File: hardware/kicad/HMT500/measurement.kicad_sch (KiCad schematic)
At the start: 15 parts, among them J3 Feedthrough 6P, U5 PCAP04-AQFM-24, U6 ADS1220IPWR

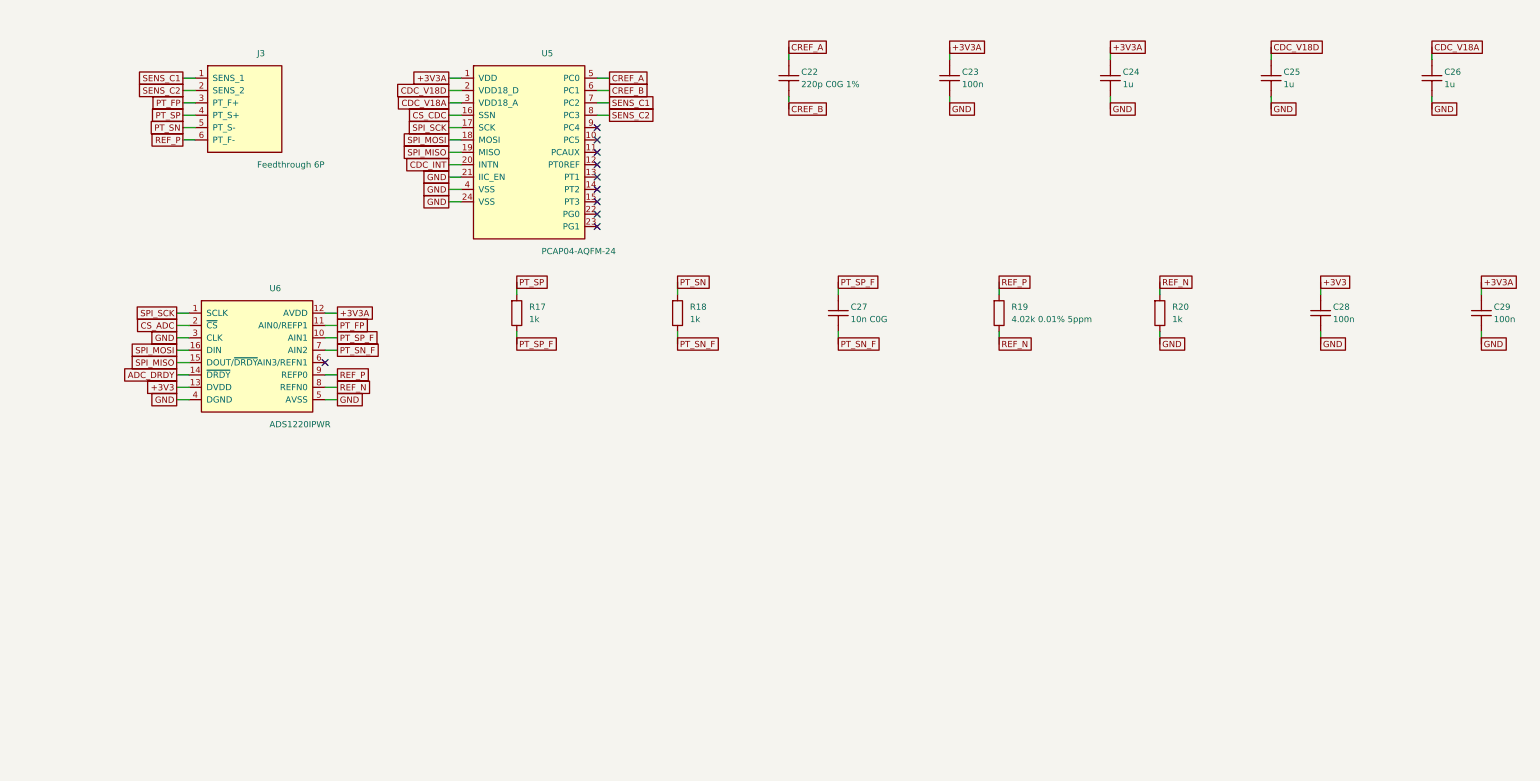
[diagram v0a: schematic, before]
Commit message: KiCad schematic v0.2: hand-laid-out, wired, readable sheets with power symbols and functional blocks
Replaces the label-only v0.1. Drawing rules are validated at generation and
the drawn netlist is checked against design intent (71 nets, 0 errors).

Co-Authored-By: Claude Opus 5.5 <noreply@anthropic.com>
Claude-Session: https://claude.ai/code/session_01JA2o8uJsqp9Vzsg4b665ev
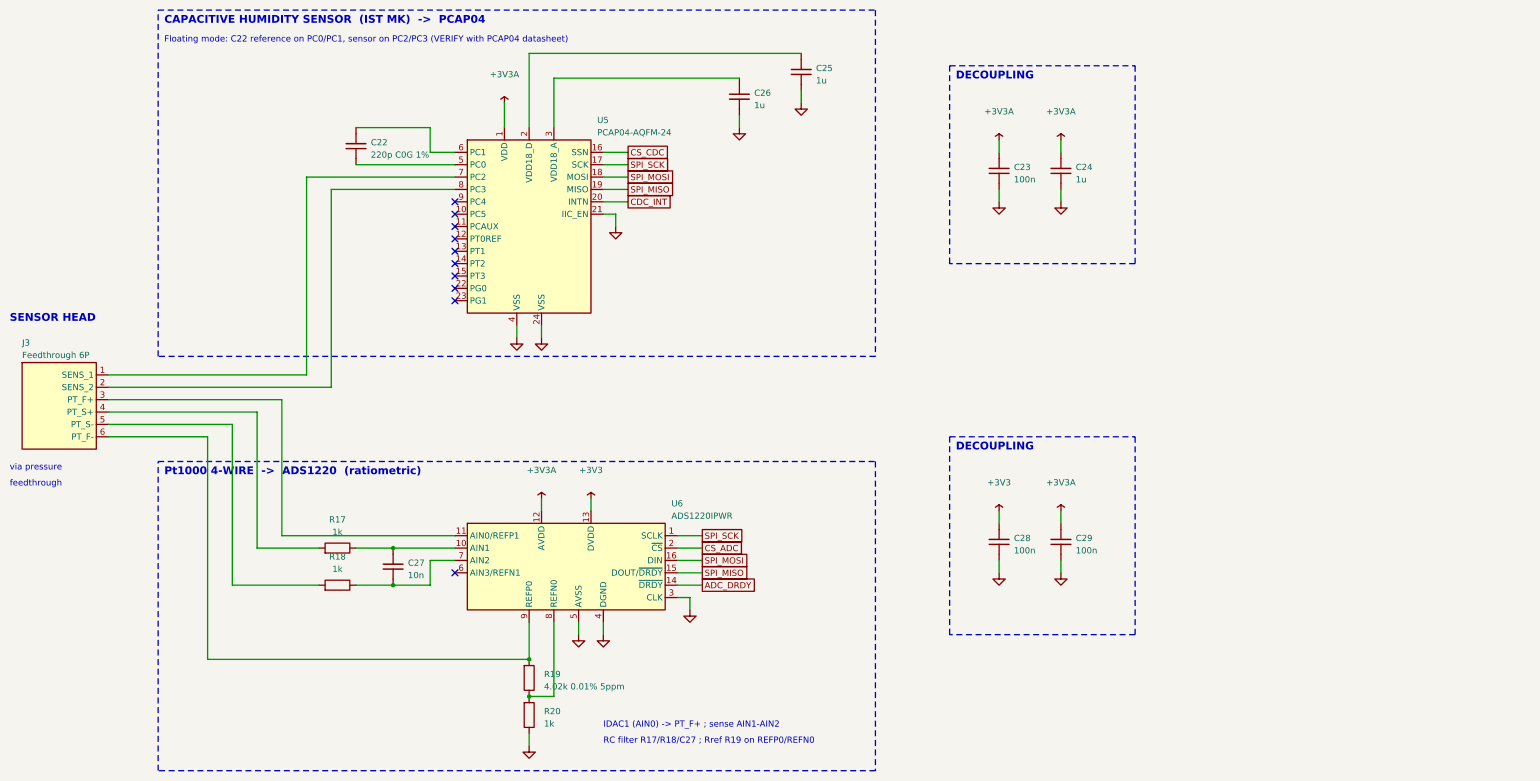
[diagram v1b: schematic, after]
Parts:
- C27: value 10n C0G -> 10n
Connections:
- net CDC_V18A: no longer names the net of C26.1, U5.3 (VDD18_A)
- net CDC_V18D: no longer names the net of C25.1, U5.2 (VDD18_D)
- net CREF_A: no longer names the net of C22.1
- net CREF_A: now also U5.6 (PC1); no longer U5.5 (PC0)
- net CREF_B: no longer names the net of C22.2
- net CREF_B: now also U5.5 (PC0); no longer U5.6 (PC1)
- net PT_FP: no longer names the net of J3.3 (PT_F+), U6.11 (AIN0/REFP1)
- net PT_SN: no longer names the net of J3.5 (PT_S-), R18.1
- net PT_SN_F: no longer names the net of C27.2, R18.2, U6.7 (AIN2)
- net PT_SP: no longer names the net of J3.4 (PT_S+), R17.1
- net PT_SP_F: no longer names the net of C27.1, R17.2, U6.10 (AIN1)
- net REF_N: no longer names the net of R19.2, R20.1, U6.8 (REFN0)
- net REF_P: no longer names the net of J3.6 (PT_F-), R19.1, U6.9 (REFP0)
- net SENS_C1: no longer names the net of J3.1 (SENS_1), U5.7 (PC2)
- net SENS_C2: no longer names the net of J3.2 (SENS_2), U5.8 (PC3)
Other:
- note added: "CAPACITIVE HUMIDITY SENSOR (IST MK) -> PCAP04"
- note added: "DECOUPLING"
- note added: "Floating mode: C22 reference on PC0/PC1, sensor on PC2/PC3 (VERIFY with PCAP04 datasheet)"
- note added: "IDAC1 (AIN0) -> PT_F+ ; sense AIN1-AIN2"
- note added: "Pt1000 4-WIRE -> ADS1220 (ratiometric)"
- note added: "RC filter R17/R18/C27 ; Rref R19 on REFP0/REFN0"
- note added: "SENSOR HEAD"
- note added: "feedthrough"
- note added: "via pressure"
- title: HMT500 - Capacitance (PCAP04) and Pt1000 (ADS1220) -> HMT500  Measurement
- moved on the sheet: C22, C23, C24, C25, C26, C27, C28, C29, J3, R17, R18, R19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

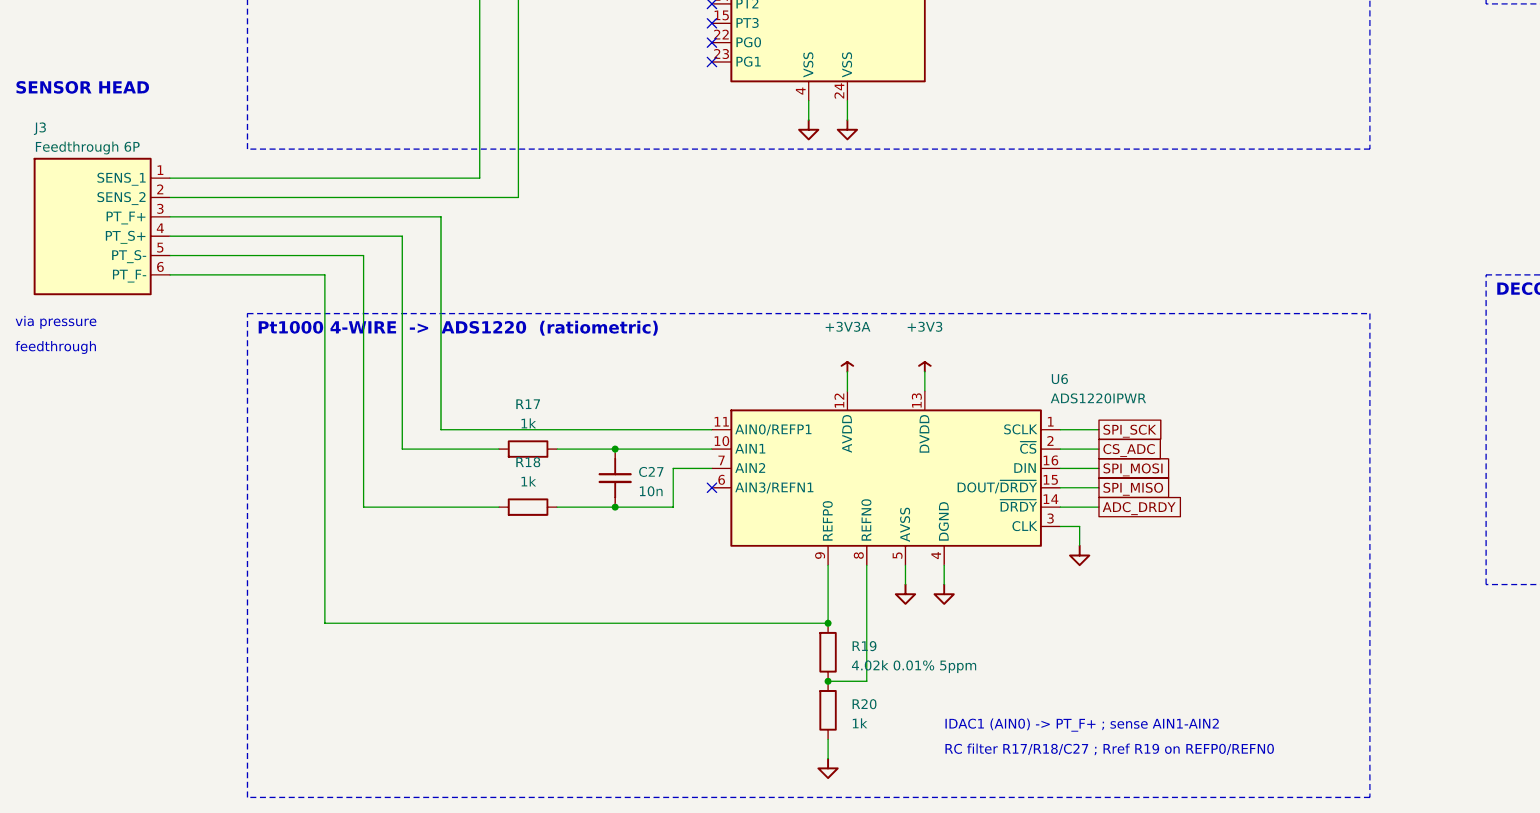
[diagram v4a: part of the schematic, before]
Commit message: Sensor harness W-1: JST SH 1.0 mm 4P between feedthrough and PCB J3
- Schematic v0.4: J3 = BM04B-SRSS-TB (top entry). Pins 1-2 MK33, 3-4 Pt1000
  2-wire with force/sense split at the J3 pads (68 nets, netlist check 0 errors)
- Parts list: J3 header, SHR-04V-S housing, SSH-003T-P0.2-H contacts, PTFE AWG30 wire
- Mech: J3 and harness in params/CAD/drawings (item 17, notes 5 and 9), PCAP04
  moved directly behind J3, PCB outline and KiCad board zone updated
- Test for harness clearance, J3 height and pin mapping
- Decision log #16; JST SH -25..+85 C rating added to open items

Co-Authored-By: Claude Opus 5.5 <noreply@anthropic.com>
Claude-Session: https://claude.ai/code/session_01JA2o8uJsqp9Vzsg4b665ev
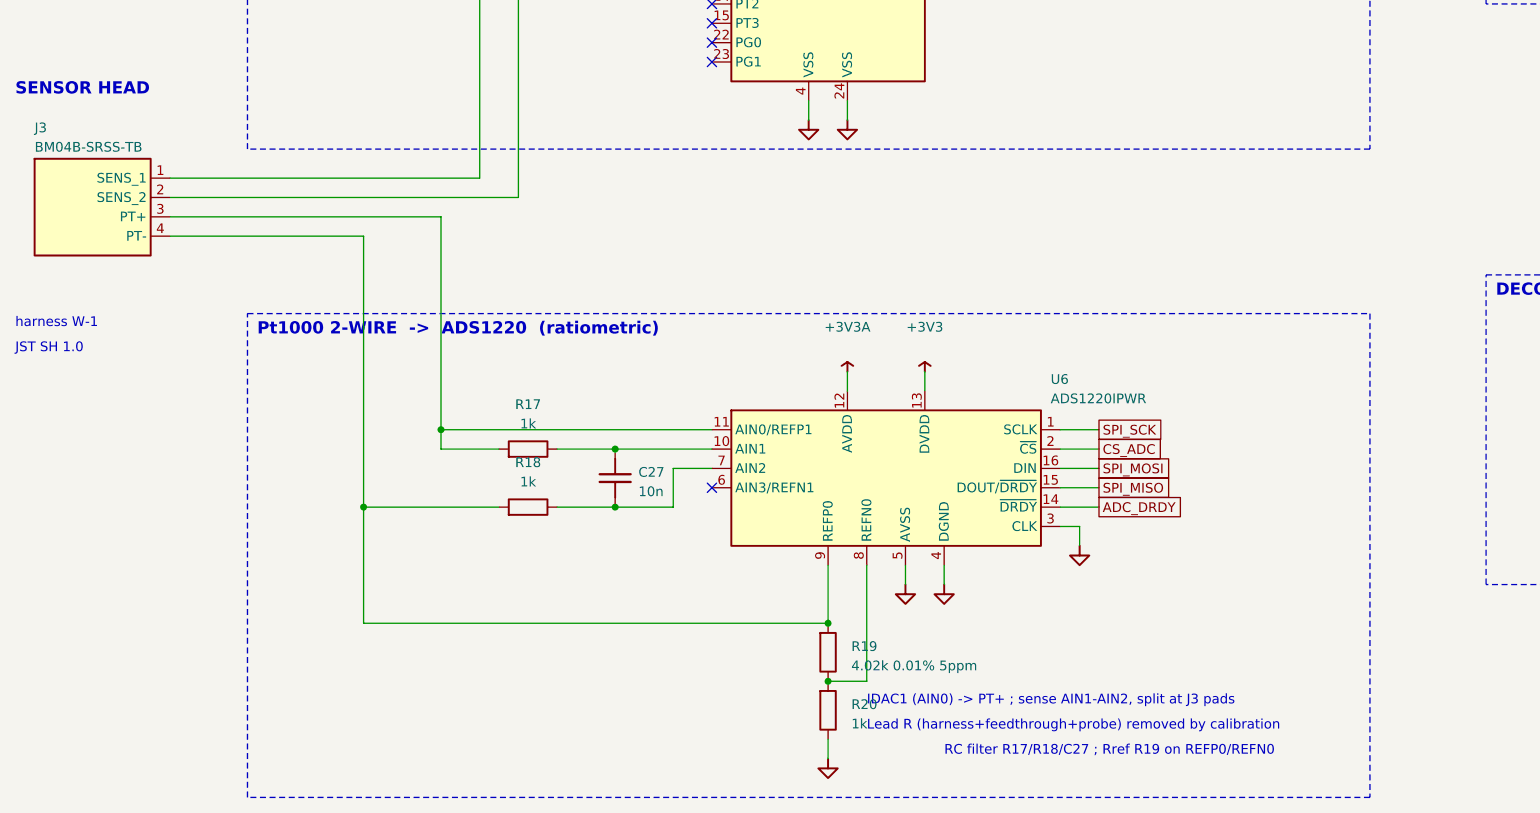
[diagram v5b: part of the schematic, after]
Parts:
- J3: value Feedthrough 6P -> BM04B-SRSS-TB; footprint TBD:Feedthrough_6P -> Connector_JST:JST_SH_BM04B-SRSS-TB_1x04-1MP_P1.00mm_Vertical; symbol HMT500:CONN_PROBE -> HMT500:CONN_SH4
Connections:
- net at J3.3 (PT+), U6.11 (AIN0/REFP1): now also R17.1
- net at R19.1, U6.9 (REFP0): now also J3.4 (PT-), R18.1; no longer J3.6 (PT_F-)
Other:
- note added: "IDAC1 (AIN0) -> PT+ ; sense AIN1-AIN2, split at J3 pads"
- note added: "JST SH 1.0"
- note added: "Lead R (harness+feedthrough+probe) removed by calibration"
- note added: "Pt1000 2-WIRE -> ADS1220 (ratiometric)"
- note added: "harness W-1"
- note removed: "IDAC1 (AIN0) -> PT_F+ ; sense AIN1-AIN2"
- note removed: "Pt1000 4-WIRE -> ADS1220 (ratiometric)"
- note removed: "feedthrough"
- note removed: "via pressure"
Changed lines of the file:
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@@
 (kicad_sch (version 20230121) (generator eeschema) (paper "A3")
-(title_block (title "HMT500  Measurement") (date "2026-09-26") (rev "0.3") (company "DOTECH Co., Ltd.") (comment 1 "Oil moisture transmitter HMT500 - RS-485 + 2x V/I analog output") (comment 2 "Design notes: docs/hw/circuit-design.md") (comment 3 "VERIFY=YES parts: pin numbers LMR36006/PCAP04/DAC8760/TPS26611; TPS2660 R22"))
-(symbol (lib_id "HMT500:CONN_PROBE") (at 25.4 106.68 0) (unit 1) (in_bom yes) (on_board yes) (dnp no) (property "Reference" "J3" (at 17.78 94.996 0) (effects (font (size 1.27 1.27)) (justify left))) (property "Value" "Feedthrough 6P" (at 17.78 97.536 0) (effects (font (size 1.27 1.27)) (justify left))) (property "Footprint" "TBD:Feedthrough_6P" (at 25.4 106.68 0) (effects (font (size 1.27 1.27)) hide)) (property "Datasheet" "~" (at 25.4 106.68 0) (effects (font (size 1.27 1.27)) hide)) (pin "1") (pin "2") (pin "3") (pin "4") (pin "5") (pin "6") (instances (project "HMT500" (path "/1ebb025b-11bd-5f7c-aaab-41e2a750e8b3/3db4a209-237d-57e2-bca4-a1eda7d94116" (reference "J3") (unit 1)))))
+(title_block (title "HMT500  Measurement") (date "2026-09-29") (rev "0.4") (company "DOTECH Co., Ltd.") (comment 1 "Oil moisture transmitter HMT500 - RS-485 + 2x V/I analog output") (comment 2 "Design notes: docs/hw/circuit-design.md") (comment 3 "VERIFY=YES parts: pin numbers LMR36006/PCAP04/DAC8760/TPS26611; TPS2660 R22"))
+(symbol (lib_id "HMT500:CONN_SH4") (at 25.4 104.14 0) (unit 1) (in_bom yes) (on_board yes) (dnp no) (property "Reference" "J3" (at 17.78 94.996 0) (effects (font (size 1.27 1.27)) (justify left))) (property "Value" "BM04B-SRSS-TB" (at 17.78 97.536 0) (effects (font (size 1.27 1.27)) (justify left))) (property "Footprint" "Connector_JST:JST_SH_BM04B-SRSS-TB_1x04-1MP_P1.00mm_Vertical" (at 25.4 104.14 0) (effects (font (size 1.27 1.27)) hide)) (property "Datasheet" "~" (at 25.4 104.14 0) (effects (font (size 1.27 1.27)) hide)) (pin "1") (pin "2") (pin "3") (pin "4") (instances (project "HMT500" (path "/1ebb025b-11bd-5f7c-aaab-41e2a750e8b3/3db4a209-237d-57e2-bca4-a1eda7d94116" (reference "J3") (unit 1)))))
 (symbol (lib_id "HMT500:PCAP04") (at 121.92 71.12 0) (unit 1) (in_bom yes) (on_board yes) (dnp no) (property "Reference" "U5" (at 135.89 49.276 0) (effects (font (size 1.27 1.27)) (justify left))) (property "Value" "PCAP04-AQFM-24" (at 135.89 51.816 0) (effects (font (size 1.27 1.27)) (justify left))) (property "Footprint" "TBD:QFN-24_PCAP04" (at 121.92 71.12 0) (effects (font (size 1.27 1.27)) hide)) (property "Datasheet" "~" (at 121.92 71.12 0) (effects (font (size 1.27 1.27)) hide)) (property "VERIFY" "YES - pin numbers are placeholders" (at 121.92 71.12 0) (effects (font (size 1.27 1.27)) hide)) (pin "6") (pin "5") (pin "7") (pin "8") (pin "9") (pin "10") (pin "11") (pin "12") (pin "13") (pin "14") (pin "15") (pin "22") (pin "23") (pin "16") (pin "17") (pin "18") (pin "19") (pin "20") (pin "21") (pin "1") (pin "2") (pin "3") (pin "4") (pin "24") (instances (project "HMT500" (path "/1ebb025b-11bd-5f7c-aaab-41e2a750e8b3/3db4a209-237d-57e2-bca4-a1eda7d94116" (reference "U5") (unit 1)))))
 (symbol (lib_id "HMT500:C") (at 86.36 54.61 0) (unit 1) (in_bom yes) (on_board yes) (dnp no) (property "Reference" "C22" (at 89.408 53.848 0) (effects (font (size 1.27 1.27)) (justify left))) (property "Value" "220p C0G 1%" (at 89.408 56.388 0) (effects (font (size 1.27 1.27)) (justify left))) (property "Footprint" "Capacitor_SMD:C_0603_1608Metric" (at 86.36 54.61 0) (effects (font (size 1.27 1.27)) hide)) (property "Datasheet" "~" (at 86.36 54.61 0) (effects (font (size 1.27 1.27)) hide)) (pin "1") (pin "2") (instances (project "HMT500" (path "/1ebb025b-11bd-5f7c-aaab-41e2a750e8b3/3db4a209-237d-57e2-bca4-a1eda7d94116" (reference "C22") (unit 1)))))
@@
 (wire (pts (xy 71.12 106.68) (xy 71.12 134.62)) (stroke (width 0) (type default)))
 (wire (pts (xy 71.12 134.62) (xy 106.68 134.62)) (stroke (width 0) (type default)))
-(wire (pts (xy 35.56 109.22) (xy 66.04 109.22)) (stroke (width 0) (type default)))
-(wire (pts (xy 66.04 109.22) (xy 66.04 137.16)) (stroke (width 0) (type default)))
-(wire (pts (xy 66.04 137.16) (xy 78.74 137.16)) (stroke (width 0) (type default)))
-(wire (pts (xy 35.56 111.76) (xy 60.96 111.76)) (stroke (width 0) (type default)))
-(wire (pts (xy 60.96 111.76) (xy 60.96 144.78)) (stroke (width 0) (type default)))
+(wire (pts (xy 71.12 134.62) (xy 71.12 137.16)) (stroke (width 0) (type default)))
+(wire (pts (xy 71.12 137.16) (xy 78.74 137.16)) (stroke (width 0) (type default)))
+(wire (pts (xy 35.56 109.22) (xy 60.96 109.22)) (stroke (width 0) (type default)))
+(wire (pts (xy 60.96 109.22) (xy 60.96 144.78)) (stroke (width 0) (type default)))
 (wire (pts (xy 60.96 144.78) (xy 78.74 144.78)) (stroke (width 0) (type default)))
+(wire (pts (xy 60.96 144.78) (xy 60.96 160.02)) (stroke (width 0) (type default)))
 (wire (pts (xy 86.36 137.16) (xy 93.98 137.16)) (stroke (width 0) (type default)))
 (wire (pts (xy 93.98 137.16) (xy 106.68 137.16)) (stroke (width 0) (type default)))
@@
 (wire (pts (xy 101.6 139.7) (xy 106.68 139.7)) (stroke (width 0) (type default)))
 (wire (pts (xy 121.92 175.26) (xy 121.92 177.8)) (stroke (width 0) (type default)))
-(wire (pts (xy 35.56 114.3) (xy 55.88 114.3)) (stroke (width 0) (type default)))
-(wire (pts (xy 55.88 114.3) (xy 55.88 160.02)) (stroke (width 0) (type default)))
-(wire (pts (xy 55.88 160.02) (xy 121.92 160.02)) (stroke (width 0) (type default)))
+(wire (pts (xy 60.96 160.02) (xy 121.92 160.02)) (stroke (width 0) (type default)))
 (wire (pts (xy 121.92 152.4) (xy 121.92 160.02)) (stroke (width 0) (type default)))
 (wire (pts (xy 121.92 167.64) (xy 127 167.64)) (stroke (width 0) (type default)))
@@
 (no_connect (at 106.68 86.36))
 (no_connect (at 106.68 142.24))
+(junction (at 60.96 144.78) (diameter 0) (color 0 0 0 0))
+(junction (at 71.12 134.62) (diameter 0) (color 0 0 0 0))
 (junction (at 93.98 137.16) (diameter 0) (color 0 0 0 0))
 (junction (at 93.98 144.78) (diameter 0) (color 0 0 0 0))
@@
 (rectangle (start 208.28 114.3) (end 246.38 154.94) (stroke (width 0.1524) (type dash) (color 72 72 160 1)) (fill (type none)))
 (text "SENSOR HEAD" (at 15.24 90.932 0) (effects (font (size 1.6 1.6) bold) (justify left bottom)))
-(text "via pressure" (at 15.24 121.412 0) (effects (font (size 1.27 1.27)) (justify left bottom)))
-(text "feedthrough" (at 15.24 124.714 0) (effects (font (size 1.27 1.27)) (justify left bottom)))
+(text "harness W-1" (at 15.24 121.412 0) (effects (font (size 1.27 1.27)) (justify left bottom)))
+(text "JST SH 1.0" (at 15.24 124.714 0) (effects (font (size 1.27 1.27)) (justify left bottom)))
 (text "CAPACITIVE HUMIDITY SENSOR  (IST MK)  ->  PCAP04" (at 46.99 29.718 0) (effects (font (size 1.6 1.6) bold) (justify left bottom)))
 (text "Floating mode: C22 reference on PC0/PC1, sensor on PC2/PC3 (VERIFY with PCAP04 datasheet)" (at 46.99 33.528 0) (effects (font (size 1.27 1.27)) (justify left bottom)))
-(text "Pt1000 4-WIRE  ->  ADS1220  (ratiometric)" (at 46.99 122.428 0) (effects (font (size 1.6 1.6) bold) (justify left bottom)))
-(text "IDAC1 (AIN0) -> PT_F+ ; sense AIN1-AIN2" (at 137.16 174.244 0) (effects (font (size 1.27 1.27)) (justify left bottom)))
+(text "Pt1000 2-WIRE  ->  ADS1220  (ratiometric)" (at 46.99 122.428 0) (effects (font (size 1.6 1.6) bold) (justify left bottom)))
+(text "IDAC1 (AIN0) -> PT+ ; sense AIN1-AIN2, split at J3 pads" (at 127 170.942 0) (effects (font (size 1.27 1.27)) (justify left bottom)))
+(text "Lead R (harness+feedthrough+probe) removed by calibration" (at 127 174.244 0) (effects (font (size 1.27 1.27)) (justify left bottom)))
 (text "RC filter R17/R18/C27 ; Rref R19 on REFP0/REFN0" (at 137.16 177.546 0) (effects (font (size 1.27 1.27)) (justify left bottom)))
 (text "DECOUPLING" (at 209.55 41.148 0) (effects (font (size 1.6 1.6) bold) (justify left bottom)))
